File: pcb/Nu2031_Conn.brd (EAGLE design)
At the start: 22.9 x 55.9 mm, 2 parts, among them X1 2520-

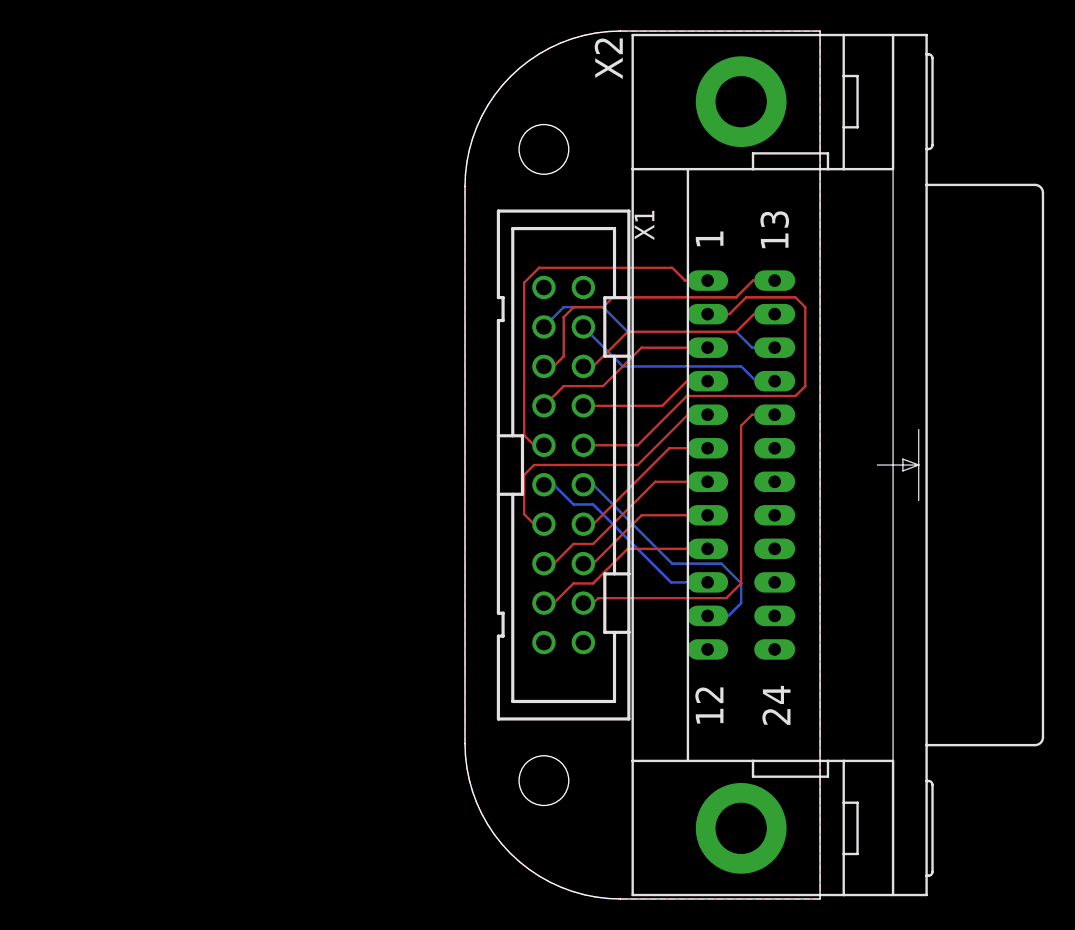
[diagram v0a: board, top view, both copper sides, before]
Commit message: First working config
* Fix some of the IEEE logic in HDL
* Add resistor to ROM selection, to default to IEC
* Add patched 1541 (2031-ish) DOS
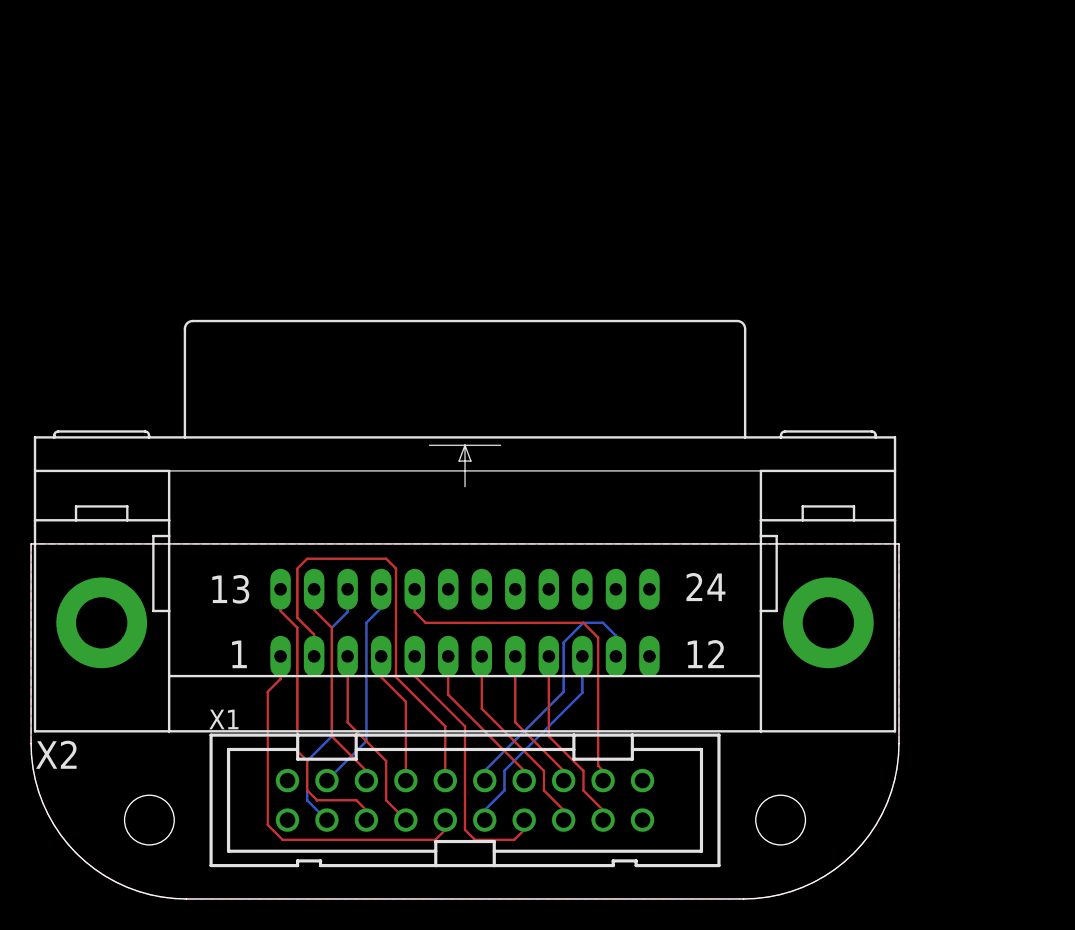
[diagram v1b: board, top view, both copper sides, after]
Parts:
- moved X1 22.5 mm to (0.00, 6.35), turned to 0 degrees
- moved X2 20.5 mm to (0.00, 17.8), turned to 0 degrees
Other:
- board size 22.9 x 55.9 mm -> 55.9 x 22.9 mm
